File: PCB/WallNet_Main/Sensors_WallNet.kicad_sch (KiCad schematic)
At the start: 45 parts, among them J201 Conn_01x04_Pin, J202 Conn_01x07_Socket, J203 Conn_02x12_Counter_Clockwise, Q201 BSS138, U201 CPT-9019B-SMT-TR, U202 SAM-M10Q-00B

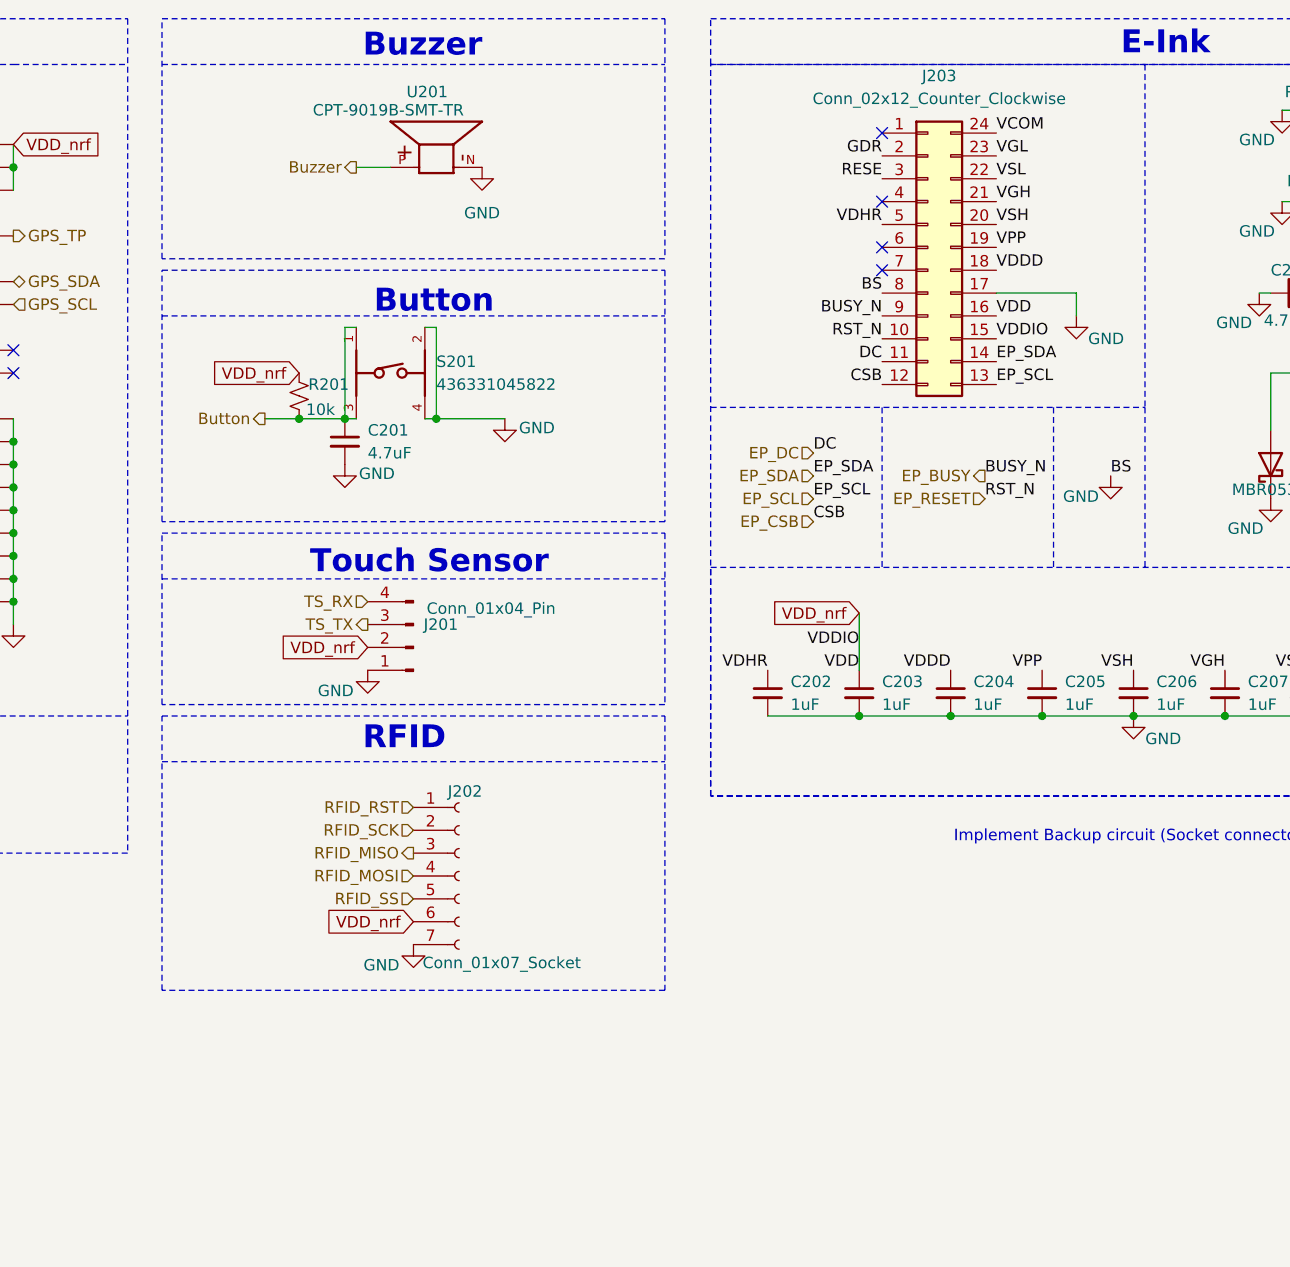
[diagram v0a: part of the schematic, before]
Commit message: updated connectors, added layout guide
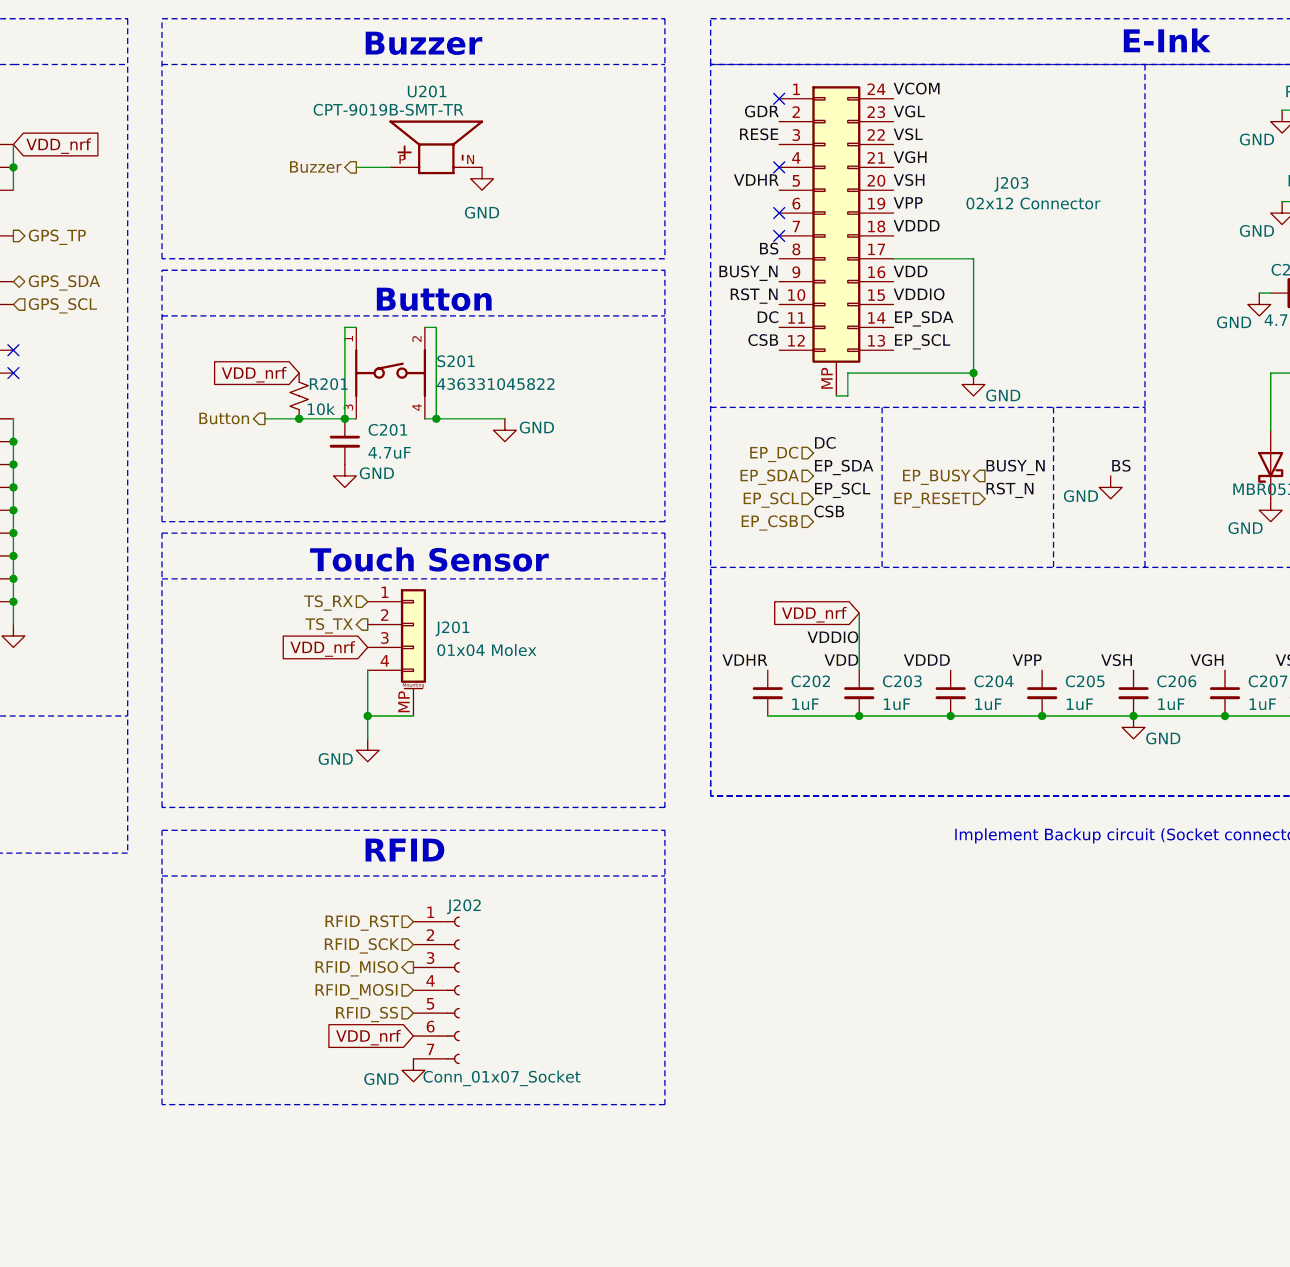
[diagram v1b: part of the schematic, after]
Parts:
- removed J201: Conn_01x04_Pin, Connector_Molex:Molex_PicoBlade_53261-0471_1x04-1MP_P1.25mm_Horizontal, symbol Connector:Conn_01x04_Pin
- added J201: 01x04 Molex, Connector_Molex:Molex_PicoBlade_53261-0471_1x04-1MP_P1.25mm_Horizontal, symbol Connector_Generic_MountingPin:Conn_01x04_MountingPin
- J203: value Conn_02x12_Counter_Clockwise -> 02x12 Connector
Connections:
- net GND: now also J203.MP (Pin_12), J201.4 (Pin_4), J201.MP (MountPin)
- net TS_RX: now also J201.1 (Pin_1)
- net TS_TX: now also J201.2 (Pin_2)
- net VDD_nrf: now also J201.3 (Pin_3)
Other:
- moved on the sheet: J202

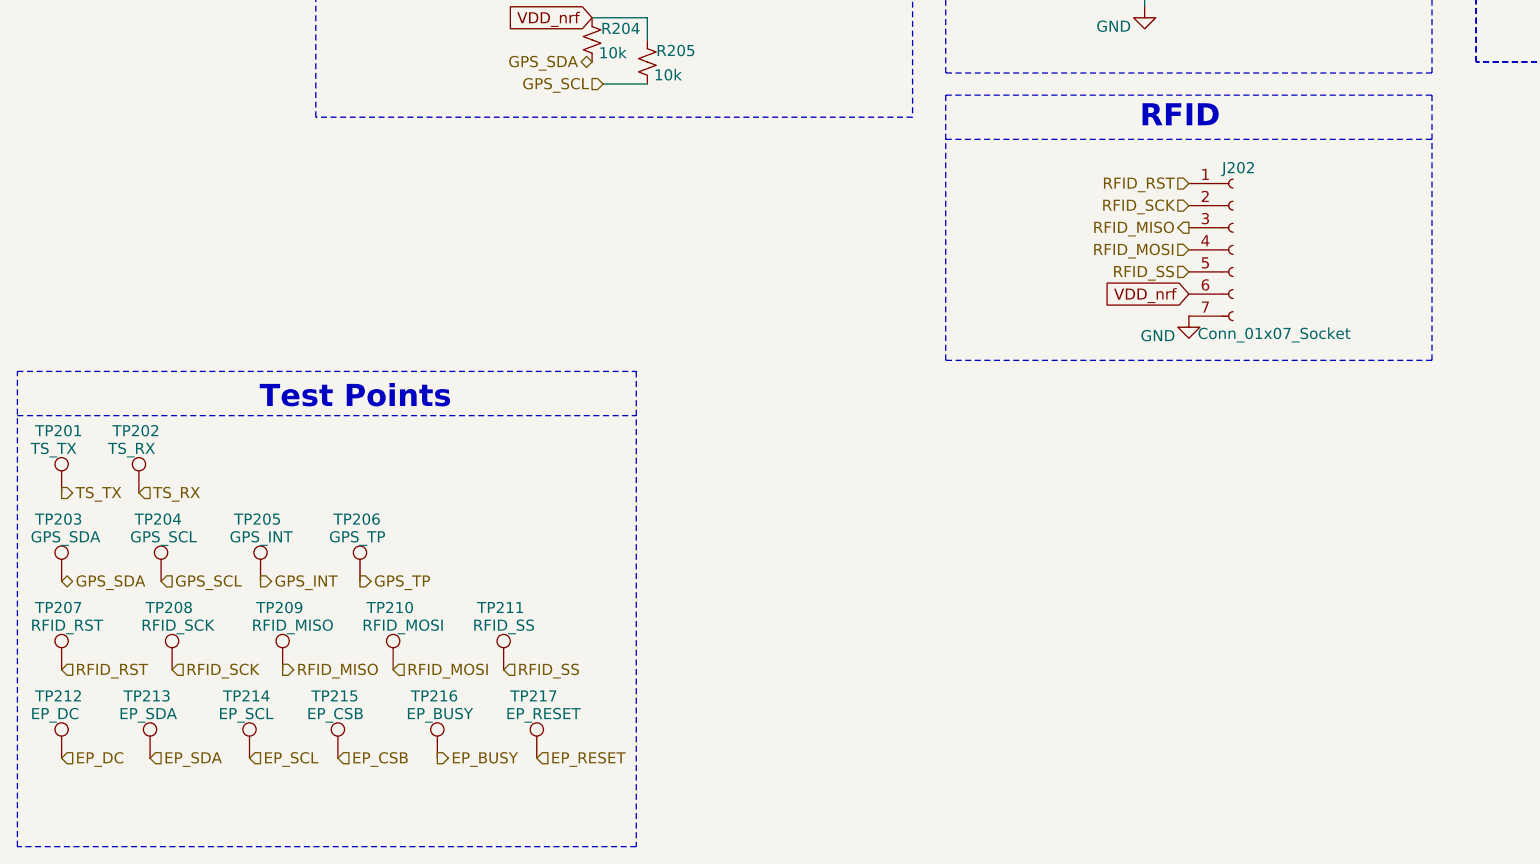
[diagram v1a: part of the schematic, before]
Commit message: Finished adding cutout, via, and mount hole for RFID
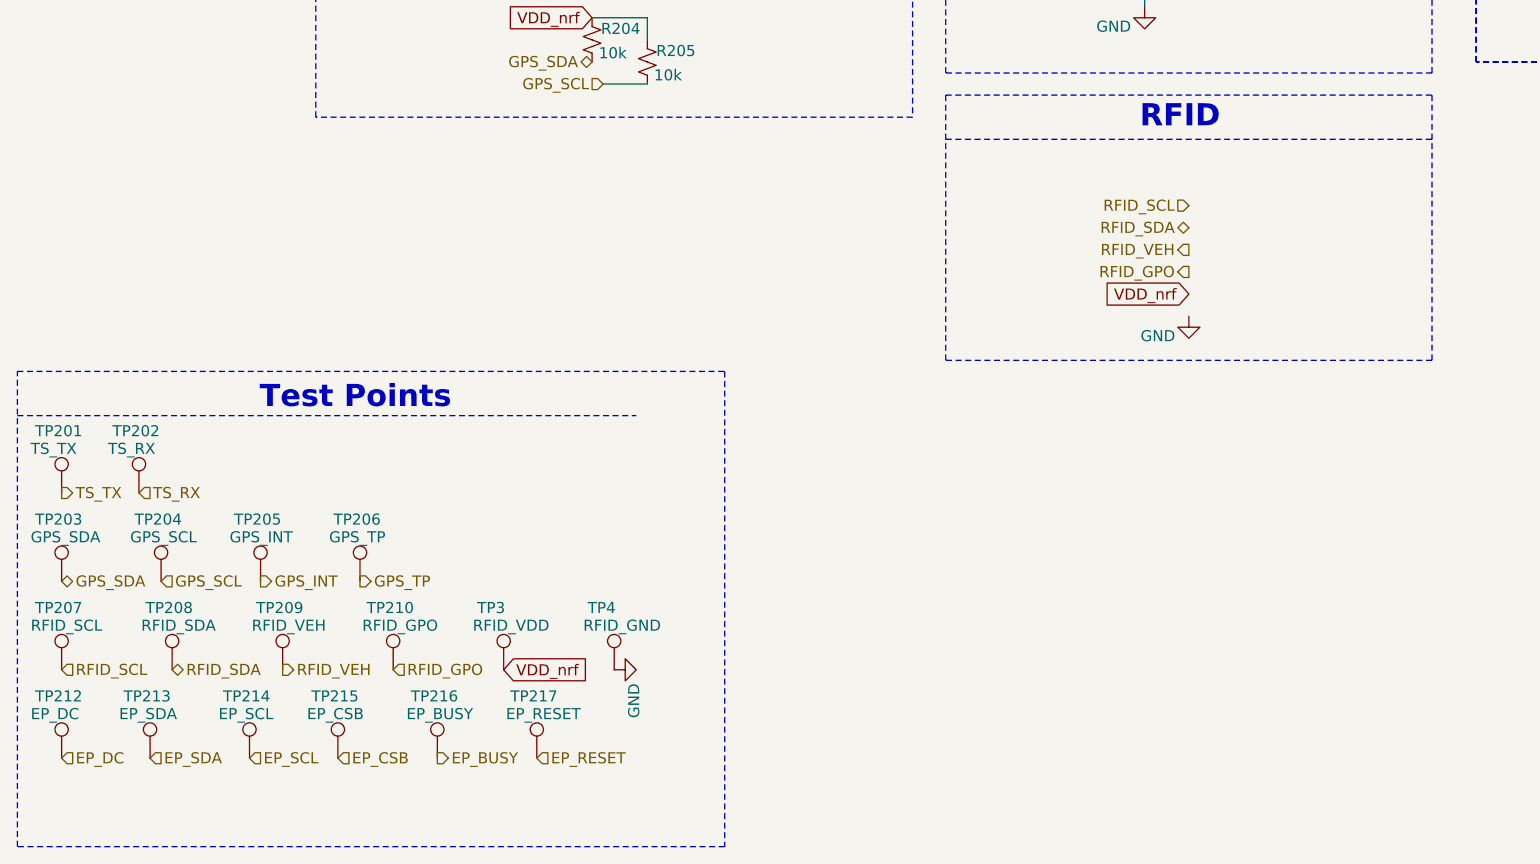
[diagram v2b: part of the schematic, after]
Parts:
- removed J202: Conn_01x07_Socket, Connector_PinSocket_2.00mm:PinSocket_1x07_P2.00mm_Horizontal, symbol Connector:Conn_01x07_Socket
- removed TP211: RFID_SS, 5001:KEYSTONE_5001, symbol Connector:TestPoint
- added TP3: RFID_VDD, 5001:KEYSTONE_5001, symbol Connector:TestPoint
- added TP4: RFID_GND, 5001:KEYSTONE_5001, symbol Connector:TestPoint
- TP207: value RFID_RST -> RFID_SCL
- TP208: value RFID_SCK -> RFID_SDA
- TP209: value RFID_MISO -> RFID_VEH
- TP210: value RFID_MOSI -> RFID_GPO
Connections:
- net GND: now also TP4.1
- net VDD_nrf: now also TP3.1
- net RFID_MISO renamed RFID_VEH
- net RFID_MOSI renamed RFID_GPO
- net RFID_RST renamed RFID_SCL
- net RFID_SCK renamed RFID_SDA
